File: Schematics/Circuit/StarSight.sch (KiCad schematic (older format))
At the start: 34 parts, among them IC1 LM2956-5V, J1 Conn_02x20_Odd_Even, J10 IR1, J11 IR1, J12 ultSound1, J13 ultSound1, J14 ultSound1, J15 ultSound1, J16 Conn_01x02, J17 Conn_01x03, J2 Line1, J3 Line2, J4 Line3, J5 Line4, J6 Line5, J7 IR1, J8 IR1, J9 IR1, P2 Power, Q4 BUZZ TO220

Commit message: Edit circuit exports
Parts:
- added J22: Conn_01x08, Pin_Headers:Pin_Header_Straight_1x08_Pitch2.54mm, symbol Conn_01x08
- J18: renamed from J?; footprint (none) -> Pin_Headers:Pin_Header_Straight_1x19_Pitch2.54mm
- J19: renamed from J?; footprint (none) -> Pin_Headers:Pin_Header_Straight_1x04_Pitch2.54mm
- J20: renamed from J?; footprint (none) -> Pin_Headers:Pin_Header_Straight_1x09_Pitch2.54mm
- J21: renamed from J?; footprint (none) -> Pin_Headers:Pin_Header_Straight_1x12_Pitch2.54mm
- R1, R2: renamed from R?; footprint (none) -> Resistors_THT:R_Axial_DIN0309_L9.0mm_D3.2mm_P12.70mm_Horizontal
- R5, R6: footprint Resistors_THT:R_Axial_DIN0414_L11.9mm_D4.5mm_P20.32mm_Horizontal -> Resistors_THT:R_Axial_DIN0309_L9.0mm_D3.2mm_P12.70mm_Horizontal
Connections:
- net at SHIELD1.10: now also J22.6 (Pin_6)
- net at SHIELD1.11: now also J22.5 (Pin_5)
- net at SHIELD1.12: now also J22.4 (Pin_4)
- net at SHIELD1.13: now also J22.3 (Pin_3)
- net at SHIELD1.8: now also J22.8 (Pin_8)
- net at SHIELD1.9: now also J22.7 (Pin_7)
- net at SHIELD1.AREF: now also J22.1 (Pin_1)
- net at SHIELD1.GND3: now also J22.2 (Pin_2)
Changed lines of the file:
@@
 F 0 "R6" V 11830 3350 50  0000 C CNN
 F 1 "100" V 11750 3350 50  0000 C CNN
-F 2 "Resistors_THT:R_Axial_DIN0414_L11.9mm_D4.5mm_P20.32mm_Horizontal" V 11680 3350 50  0001 C CNN
+F 2 "Resistors_THT:R_Axial_DIN0309_L9.0mm_D3.2mm_P12.70mm_Horizontal" V 11680 3350 50  0001 C CNN
 F 3 "" H 11750 3350 50  0001 C CNN
 	1    11750 3350
@@
 F 0 "R5" V 11830 2750 50  0000 C CNN
 F 1 "10k" V 11750 2750 50  0000 C CNN
-F 2 "Resistors_THT:R_Axial_DIN0414_L11.9mm_D4.5mm_P20.32mm_Horizontal" V 11680 2750 50  0001 C CNN
+F 2 "Resistors_THT:R_Axial_DIN0309_L9.0mm_D3.2mm_P12.70mm_Horizontal" V 11680 2750 50  0001 C CNN
 F 3 "" H 11750 2750 50  0001 C CNN
 	1    11750 2750
@@
 	10450 5100 13100 5100
 $Comp
-L Conn_01x09 J?
+L Conn_01x09 J20
 U 1 1 5A92B9C8
 P 10050 5050
-F 0 "J?" H 10050 5550 50  0000 C CNN
+F 0 "J20" H 10050 5550 50  0000 C CNN
 F 1 "Conn_01x09" H 10050 4550 50  0000 C CNN
-F 2 "" H 10050 5050 50  0001 C CNN
+F 2 "Pin_Headers:Pin_Header_Straight_1x09_Pitch2.54mm" H 10050 5050 50  0001 C CNN
 F 3 "" H 10050 5050 50  0001 C CNN
 	1    10050 5050
@@
 	9750 5450 9850 5450
 $Comp
-L Conn_01x04 J?
+L Conn_01x04 J19
 U 1 1 5A92CF57
 P 7350 5550
-F 0 "J?" H 7350 5750 50  0000 C CNN
+F 0 "J19" H 7350 5750 50  0000 C CNN
 F 1 "Conn_01x04" H 7350 5250 50  0000 C CNN
-F 2 "" H 7350 5550 50  0001 C CNN
+F 2 "Pin_Headers:Pin_Header_Straight_1x04_Pitch2.54mm" H 7350 5550 50  0001 C CNN
 F 3 "" H 7350 5550 50  0001 C CNN
 	1    7350 5550
@@
 V_READ
 $Comp
-L R R?
+L R R1
 U 1 1 5A92FC36
 P 4000 2350
-F 0 "R?" V 4080 2350 50  0000 C CNN
+F 0 "R1" V 4080 2350 50  0000 C CNN
 F 1 "20k" V 4000 2350 50  0000 C CNN
-F 2 "" V 3930 2350 50  0001 C CNN
+F 2 "Resistors_THT:R_Axial_DIN0309_L9.0mm_D3.2mm_P12.70mm_Horizontal" V 3930 2350 50  0001 C CNN
 F 3 "" H 4000 2350 50  0001 C CNN
 	1    4000 2350
@@
 $EndComp
 $Comp
-L R R?
+L R R2
 U 1 1 5A92FD21
 P 4000 2900
-F 0 "R?" V 4080 2900 50  0000 C CNN
+F 0 "R2" V 4080 2900 50  0000 C CNN
 F 1 "10k" V 4000 2900 50  0000 C CNN
-F 2 "" V 3930 2900 50  0001 C CNN
+F 2 "Resistors_THT:R_Axial_DIN0309_L9.0mm_D3.2mm_P12.70mm_Horizontal" V 3930 2900 50  0001 C CNN
 F 3 "" H 4000 2900 50  0001 C CNN
 	1    4000 2900
@@
 Connection ~ 3650 1800
 $Comp
-L GND-RESCUE-StarSight #PWR?
+L GND-RESCUE-StarSight #PWR018
 U 1 1 5A930057
 P 4000 3300
-F 0 "#PWR?" H 4000 3300 30  0001 C CNN
+F 0 "#PWR018" H 4000 3300 30  0001 C CNN
 F 1 "GND" H 4000 3230 30  0001 C CNN
 F 2 "" H 4000 3300 60  0000 C CNN
@@
 V_READ
 $Comp
-L Conn_01x12 J?
+L Conn_01x12 J21
 U 1 1 5A930804
 P 11150 8150
-F 0 "J?" H 11150 8750 50  0000 C CNN
+F 0 "J21" H 11150 8750 50  0000 C CNN
 F 1 "Conn_01x12" H 11150 7450 50  0000 C CNN
-F 2 "" H 11150 8150 50  0001 C CNN
+F 2 "Pin_Headers:Pin_Header_Straight_1x12_Pitch2.54mm" H 11150 8150 50  0001 C CNN
 F 3 "" H 11150 8150 50  0001 C CNN
 	1    11150 8150
@@
 $EndComp
 $Comp
-L Conn_01x19 J?
+L Conn_01x19 J18
 U 1 1 5A930887
 P 6050 8150
-F 0 "J?" H 6050 9150 50  0000 C CNN
+F 0 "J18" H 6050 9150 50  0000 C CNN
 F 1 "Conn_01x19" H 6050 7150 50  0000 C CNN
-F 2 "" H 6050 8150 50  0001 C CNN
+F 2 "Pin_Headers:Pin_Header_Straight_1x19_Pitch2.54mm" H 6050 8150 50  0001 C CNN
 F 3 "" H 6050 8150 50  0001 C CNN
 	1    6050 8150
@@
 Wire Wire Line
 	10650 8750 10950 8750
+$Comp
+L Conn_01x08 J22
+U 1 1 5A936895
+P 10100 3900
+F 0 "J22" H 10100 4300 50  0000 C CNN
+F 1 "Conn_01x08" H 10100 3400 50  0000 C CNN
+F 2 "Pin_Headers:Pin_Header_Straight_1x08_Pitch2.54mm" H 10100 3900 50  0001 C CNN
+F 3 "" H 10100 3900 50  0001 C CNN
+	1    10100 3900
+	1    0    0    -1
+$EndComp
+Wire Wire Line
+	9650 3600 9900 3600
+Wire Wire Line
+	9900 3700 9650 3700
+Wire Wire Line
+	9650 3800 9900 3800
+Wire Wire Line
+	9900 3900 9650 3900
+Wire Wire Line
+	9650 4000 9900 4000
+Wire Wire Line
+	9900 4100 9650 4100
+Wire Wire Line
+	9650 4200 9900 4200
+Wire Wire Line
+	9900 4300 9650 4300
 $EndSCHEMATC

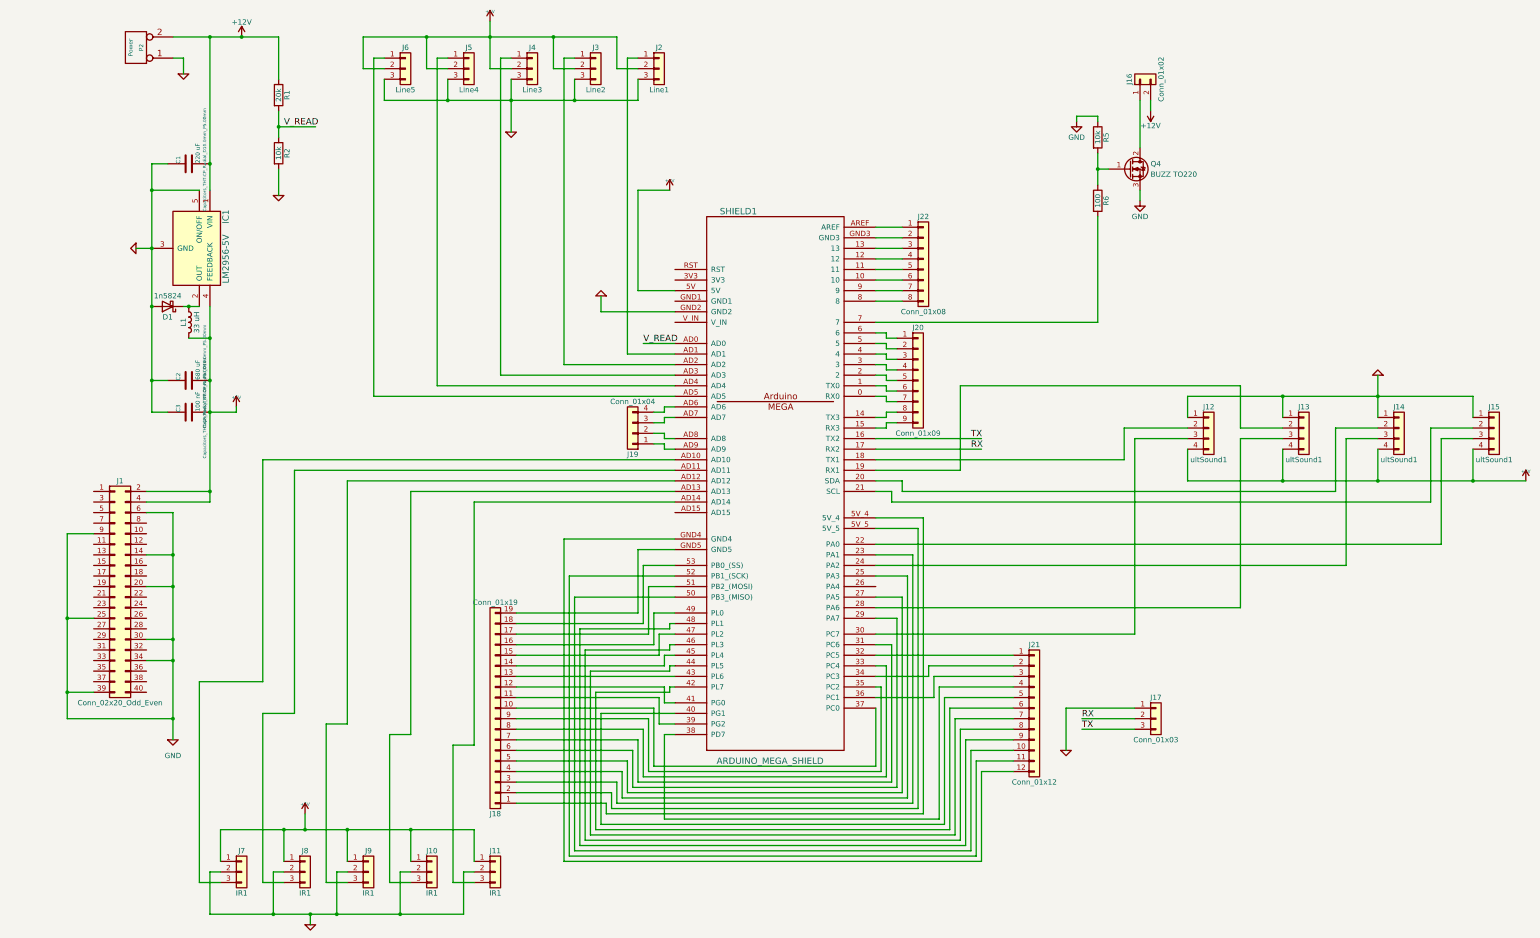
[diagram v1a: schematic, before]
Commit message: Add pins for raspberry and few circuit fixes
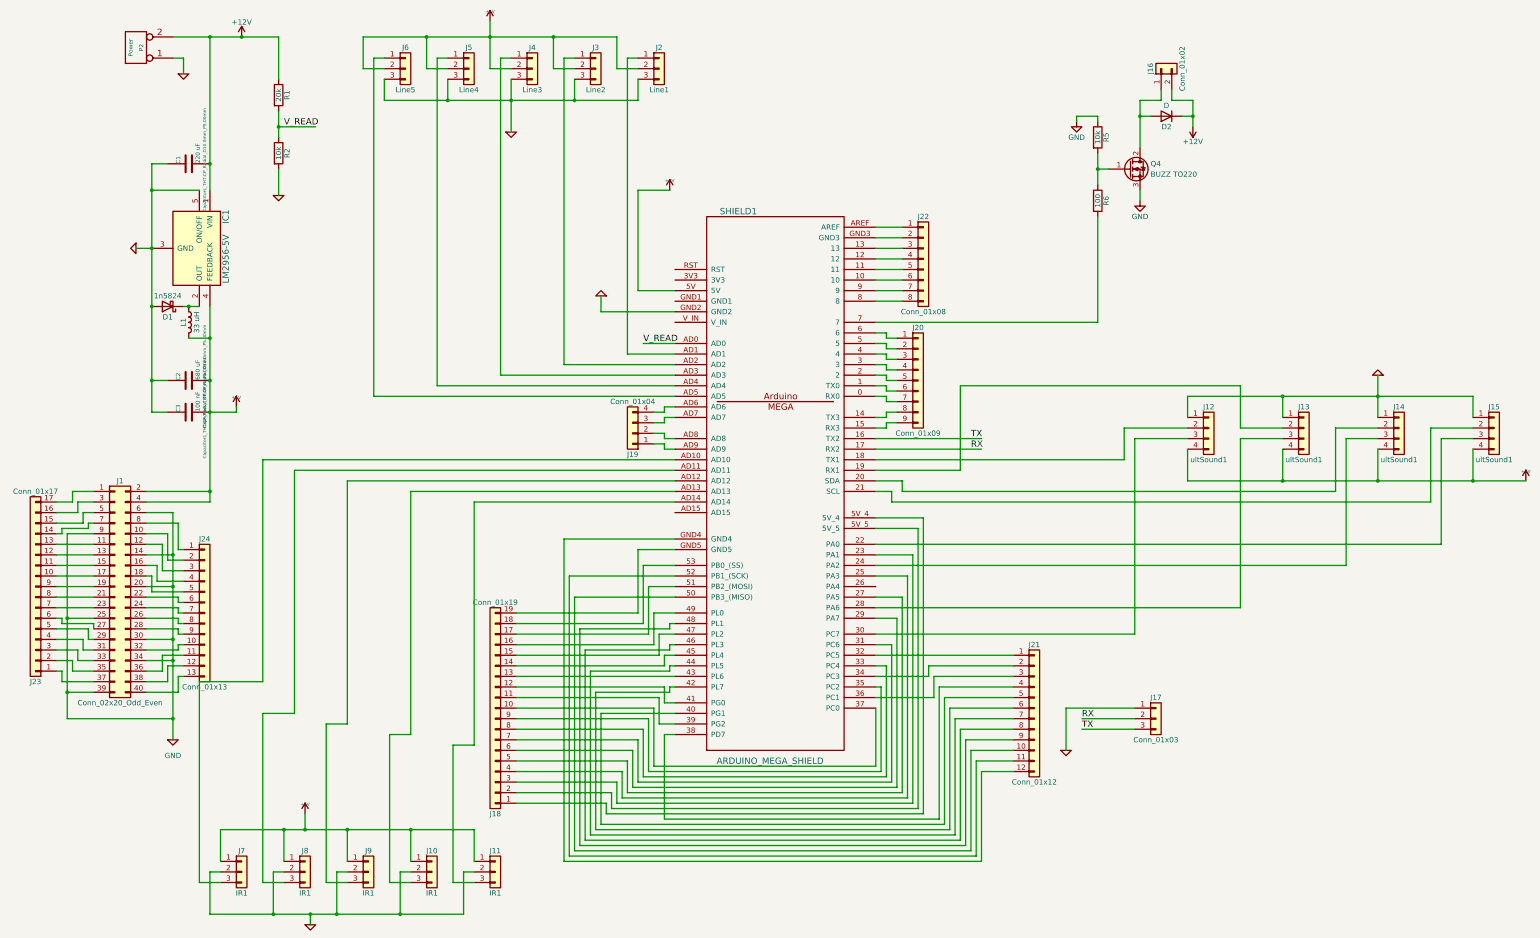
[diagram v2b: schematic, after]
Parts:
- added D2: D, Diodes_THT:D_DO-201_P15.24mm_Horizontal, symbol D
- added J23: Conn_01x17, Pin_Headers:Pin_Header_Straight_1x17_Pitch2.54mm, symbol Conn_01x17
- added J24: Conn_01x13, Pin_Headers:Pin_Header_Straight_1x13_Pitch2.54mm, symbol Conn_01x13
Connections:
- net +12V: now also D2.1 (K)
- net at J16.1 (Pin_1), Q4.2 (D): now also D2.2 (A)
- net at J1.1 (Pin_1): now also J23.17 (Pin_17)
- net at J1.10 (Pin_10): now also J24.2 (Pin_2)
- net at J1.11 (Pin_11): now also J23.13 (Pin_13)
- net at J1.12 (Pin_12): now also J24.3 (Pin_3)
- net at J1.13 (Pin_13): now also J23.12 (Pin_12)
- net at J1.15 (Pin_15): now also J23.11 (Pin_11)
- net at J1.16 (Pin_16): now also J24.4 (Pin_4)
- net at J1.17 (Pin_17): now also J23.10 (Pin_10)
- net at J1.18 (Pin_18): now also J24.5 (Pin_5)
- net at J1.19 (Pin_19): now also J23.9 (Pin_9)
- net at J1.21 (Pin_21): now also J23.8 (Pin_8)
- net at J1.22 (Pin_22): now also J24.6 (Pin_6)
- net at J1.23 (Pin_23): now also J23.7 (Pin_7)
- net at J1.24 (Pin_24): now also J24.7 (Pin_7)
- net at J1.26 (Pin_26): now also J24.8 (Pin_8)
- net at J1.27 (Pin_27): now also J23.6 (Pin_6)
- net at J1.28 (Pin_28): now also J24.9 (Pin_9)
- net at J1.29 (Pin_29): now also J23.5 (Pin_5)
- net at J1.3 (Pin_3): now also J23.16 (Pin_16)
- net at J1.31 (Pin_31): now also J23.4 (Pin_4)
- net at J1.32 (Pin_32): now also J24.10 (Pin_10)
- net at J1.33 (Pin_33): now also J23.3 (Pin_3)
- net at J1.35 (Pin_35): now also J23.2 (Pin_2)
- net at J1.36 (Pin_36): now also J24.11 (Pin_11)
- net at J1.37 (Pin_37): now also J23.1 (Pin_1)
- net at J1.38 (Pin_38): now also J24.12 (Pin_12)
- net at J1.40 (Pin_40): now also J24.13 (Pin_13)
- net at J1.5 (Pin_5): now also J23.15 (Pin_15)
- net at J1.7 (Pin_7): now also J23.14 (Pin_14)
- net at J1.8 (Pin_8): now also J24.1 (Pin_1)
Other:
- moved on the sheet: J16
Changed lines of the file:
@@
 L Conn_01x02 J16
 U 1 1 5A8B16B7
-P 12150 2200
-F 0 "J16" H 12150 2300 50  0000 C CNN
-F 1 "Conn_01x02" H 12150 2000 50  0000 C CNN
-F 2 "Connectors_Terminal_Blocks:TerminalBlock_Philmore_TB132_02x5mm_Straight" H 12150 2200 50  0001 C CNN
-F 3 "" H 12150 2200 50  0001 C CNN
-	1    12150 2200
+P 12350 2100
+F 0 "J16" H 12350 2200 50  0000 C CNN
+F 1 "Conn_01x02" H 12350 1900 50  0000 C CNN
+F 2 "Connectors_Terminal_Blocks:TerminalBlock_Philmore_TB132_02x5mm_Straight" H 12350 2100 50  0001 C CNN
+F 3 "" H 12350 2100 50  0001 C CNN
+	1    12350 2100
 	0    -1   -1   0
 $EndComp
@@
 L +12V #PWR013
 U 1 1 5A8B615B
-P 12250 2500
-F 0 "#PWR013" H 12250 2350 50  0001 C CNN
-F 1 "+12V" H 12250 2640 50  0000 C CNN
-F 2 "" H 12250 2500 50  0001 C CNN
-F 3 "" H 12250 2500 50  0001 C CNN
-	1    12250 2500
+P 12650 2650
+F 0 "#PWR013" H 12650 2500 50  0001 C CNN
+F 1 "+12V" H 12650 2790 50  0000 C CNN
+F 2 "" H 12650 2650 50  0001 C CNN
+F 3 "" H 12650 2650 50  0001 C CNN
+	1    12650 2650
 	-1   0    0    1
 $EndComp
@@
 	11550 2600 11550 2550
 Wire Wire Line
-	12250 2500 12250 2400
+	12450 2400 12450 2300
 Wire Wire Line
 	3350 6200 2750 6200
@@
 Wire Wire Line
 	9900 4300 9650 4300
+$Comp
+L Conn_01x17 J23
+U 1 1 5A932461
+P 1700 7000
+F 0 "J23" H 1700 7900 50  0000 C CNN
+F 1 "Conn_01x17" H 1700 6100 50  0000 C CNN
+F 2 "Pin_Headers:Pin_Header_Straight_1x17_Pitch2.54mm" H 1700 7000 50  0001 C CNN
+F 3 "" H 1700 7000 50  0001 C CNN
+	1    1700 7000
+	-1   0    0    1
+$EndComp
+Wire Wire Line
+	1950 7900 2250 7900
+Wire Wire Line
+	1950 7900 1950 7800
+Wire Wire Line
+	1950 7800 1900 7800
+Wire Wire Line
+	2250 7800 2050 7800
+Wire Wire Line
+	2050 7800 2050 7700
+Wire Wire Line
+	2050 7700 1900 7700
+Wire Wire Line
+	2250 7700 2100 7700
+Wire Wire Line
+	2100 7700 2100 7600
+Wire Wire Line
+	2100 7600 1900 7600
+Wire Wire Line
+	2250 7600 2150 7600
+Wire Wire Line
+	2150 7600 2150 7500
+Wire Wire Line
+	2150 7500 1900 7500
+Wire Wire Line
+	2250 7500 2200 7500
+Wire Wire Line
+	2200 7500 2200 7400
+Wire Wire Line
+	2200 7400 1900 7400
+Wire Wire Line
+	2250 7400 2250 7350
+Wire Wire Line
+	2250 7350 1950 7350
+Wire Wire Line
+	1950 7350 1950 7300
+Wire Wire Line
+	1950 7300 1900 7300
+Wire Wire Line
+	2250 7200 1900 7200
+Wire Wire Line
+	1900 7100 2250 7100
+Wire Wire Line
+	2250 7000 1900 7000
+Wire Wire Line
+	1900 6900 2250 6900
+Wire Wire Line
+	2250 6800 1900 6800
+Wire Wire Line
+	1900 6700 2250 6700
+Wire Wire Line
+	2250 6600 1900 6600
+Wire Wire Line
+	1900 6500 1950 6500
+Wire Wire Line
+	1950 6500 1950 6450
+Wire Wire Line
+	1950 6450 2200 6450
+Wire Wire Line
+	2200 6450 2200 6400
+Wire Wire Line
+	2200 6400 2250 6400
+Wire Wire Line
+	1900 6400 2150 6400
+Wire Wire Line
+	2150 6400 2150 6300
+Wire Wire Line
+	2150 6300 2250 6300
+Wire Wire Line
+	1900 6300 2100 6300
+Wire Wire Line
+	2100 6300 2100 6200
+Wire Wire Line
+	2100 6200 2250 6200
+Wire Wire Line
+	1900 6200 2050 6200
+Wire Wire Line
+	2050 6200 2050 6100
+Wire Wire Line
+	2050 6100 2250 6100
+$Comp
+L Conn_01x13 J24
+U 1 1 5A9347F5
+P 3300 7250
+F 0 "J24" H 3300 7950 50  0000 C CNN
+F 1 "Conn_01x13" H 3300 6550 50  0000 C CNN
+F 2 "Pin_Headers:Pin_Header_Straight_1x13_Pitch2.54mm" H 3300 7250 50  0001 C CNN
+F 3 "" H 3300 7250 50  0001 C CNN
+	1    3300 7250
+	1    0    0    -1
+$EndComp
+Wire Wire Line
+	2750 8000 3050 8000
+Wire Wire Line
+	3050 8000 3050 7850
+Wire Wire Line
+	3050 7850 3100 7850
+Wire Wire Line
+	2750 7900 2950 7900
+Wire Wire Line
+	2950 7900 2950 7750
+Wire Wire Line
+	2950 7750 3100 7750
+Wire Wire Line
+	2750 7800 2900 7800
+Wire Wire Line
+	2900 7800 2900 7650
+Wire Wire Line
+	2900 7650 3100 7650
+Wire Wire Line
+	2750 7600 3050 7600
+Wire Wire Line
+	3050 7600 3050 7550
+Wire Wire Line
+	3050 7550 3100 7550
+Wire Wire Line
+	2750 7400 3050 7400
+Wire Wire Line
+	3050 7400 3050 7450
+Wire Wire Line
+	3050 7450 3100 7450
+Wire Wire Line
+	3100 7350 3050 7350
+Wire Wire Line
+	3050 7350 3050 7300
+Wire Wire Line
+	3050 7300 2750 7300
+Wire Wire Line
+	3100 7250 3050 7250
+Wire Wire Line
+	3050 7250 3050 7200
+Wire Wire Line
+	3050 7200 2750 7200
+Wire Wire Line
+	2750 7100 3050 7100
+Wire Wire Line
+	3050 7100 3050 7150
+Wire Wire Line
+	3050 7150 3100 7150
+Wire Wire Line
+	3100 7050 2800 7050
+Wire Wire Line
+	2800 7050 2800 6900
+Wire Wire Line
+	2800 6900 2750 6900
+Wire Wire Line
+	2750 6800 2850 6800
+Wire Wire Line
+	2850 6800 2850 6950
+Wire Wire Line
+	2850 6950 3100 6950
+Wire Wire Line
+	3100 6850 2900 6850
+Wire Wire Line
+	2900 6850 2900 6600
+Wire Wire Line
+	2900 6600 2750 6600
+Wire Wire Line
+	3100 6750 2950 6750
+Wire Wire Line
+	2950 6750 2950 6500
+Wire Wire Line
+	2950 6500 2750 6500
+Wire Wire Line
+	3100 6650 3050 6650
+Wire Wire Line
+	3050 6650 3050 6400
+Wire Wire Line
+	3050 6400 2750 6400
+Wire Wire Line
+	12150 2400 12350 2400
+Wire Wire Line
+	12350 2400 12350 2300
+Wire Wire Line
+	12450 2400 12650 2400
+Wire Wire Line
+	12650 2400 12650 2650
+$Comp
+L D D2
+U 1 1 5A93732E
+P 12400 2550
+F 0 "D2" H 12400 2650 50  0000 C CNN
+F 1 "D" H 12400 2450 50  0000 C CNN
+F 2 "Diodes_THT:D_DO-201_P15.24mm_Horizontal" H 12400 2550 50  0001 C CNN
+F 3 "" H 12400 2550 50  0001 C CNN
+	1    12400 2550
+	-1   0    0    1
+$EndComp
+Wire Wire Line
+	12550 2550 12650 2550
+Connection ~ 12650 2550
+Wire Wire Line
+	12250 2550 12150 2550
+Connection ~ 12150 2550
 $EndSCHEMATC
